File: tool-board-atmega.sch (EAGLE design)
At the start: 101 parts, among them IC3 ATMEGA2560-16AU, IC4 ATMEGA8U2-MU, Q1 16MHz, X1 22-23-2041, X2 MICROUSB_VERTICAL, X3 22-23-2041, X4 22-23-2041, Y2 16MHz

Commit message: board Rev01 done, needs review by Jaden and to clean up labels
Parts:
- removed U$2, U$3, U$4, U$5: FIDUCIALMOUNT, SmartPrj:FIDUCIALMOUNT
- added A: 22-23-2081, con-molex:22-23-2081
- added SV1, SV2, SV3: (no value), con-lstb:MA03-1
- added X5, X6: (no value), con-phoenix-254:MPT12
- added X7: (no value), con-phoenix-254:MPT4
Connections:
- new net N$50: A-1.S, IC3.(ADC7/TDI)PF7
- new net N$51: A-2.S, IC3.(ADC6/TDO)PF6
- new net N$52: A-3.S, IC3.(ADC5/TMS)PF5
- new net N$53: A-4.S, IC3.(ADC4/TCK)PF4
- new net N$56: A-5.S, IC3.(ADC3)PF3
- new net N$57: A-6.S, IC3.(ADC2)PF2
- new net N$58: A-7.S, IC3.(ADC1)PF1
- new net N$59: A-8.S, IC3.(ADC0)PF0
- new net N$60: SV1.2, X4-2.S
- new net N$61: SV2.2, X3-2.S
- new net N$62: SV3.2, X1-2.S
- net +12V: now also SV1.1, SV2.1, SV3.1, X6-10.1, X6-11.1, X6-12.1, X6-7.1, X6-8.1, X6-9.1
- net +24V: now also X7-1.1, X7-2.1, X7-3.1, X7-4.1
- net +5V: now also SV1.3, SV2.3, SV3.3, X6-1.1, X6-2.1, X6-3.1, X6-4.1, X6-5.1, X6-6.1; no longer X1-2.S, X3-2.S, X4-2.S
- net GND: now also X5-1.1, X5-10.1, X5-11.1, X5-12.1, X5-2.1, X5-3.1, X5-4.1, X5-5.1, X5-6.1, X5-7.1, X5-8.1, X5-9.1

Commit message: Made revisions of Jaden's review
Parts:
- removed RESET-EN: (no value), jumper:SJ
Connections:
- net RESET: no longer RESET-EN.1, RESET-EN.2
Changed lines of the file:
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@@
 <part name="GND28" library="supply1" deviceset="GND" device=""/>
 <part name="C7" library="SmartPrj" deviceset="C-EU" device="0603-RND" value="100n"/>
-<part name="RESET-EN" library="jumper" deviceset="SJ" device=""/>
 <part name="GND18" library="supply1" deviceset="GND" device=""/>
 <part name="C10" library="SmartPrj" deviceset="C-EU" device="0603-RND" value="1u"/>
@@
 <attribute name="VALUE" x="530.479" y="79.756" size="1.778" layer="96" rot="MR270"/>
 </instance>
-<instance part="RESET-EN" gate="1" x="538.48" y="96.52" smashed="yes">
-<attribute name="NAME" x="533.4" y="92.71" size="1.778" layer="95"/>
-<attribute name="VALUE" x="535.94" y="92.71" size="1.778" layer="96"/>
-</instance>
 <instance part="GND18" gate="1" x="510.54" y="58.42" smashed="yes">
 <attribute name="VALUE" x="508" y="55.88" size="1.778" layer="96"/>
@@
 </segment>
 <segment>
-<wire x1="530.86" y1="81.28" x2="533.4" y2="81.28" width="0.1524" layer="91"/>
-<wire x1="533.4" y1="81.28" x2="546.1" y2="81.28" width="0.1524" layer="91"/>
-<wire x1="546.1" y1="81.28" x2="548.64" y2="81.28" width="0.1524" layer="91"/>
-<wire x1="533.4" y1="96.52" x2="533.4" y2="81.28" width="0.1524" layer="91"/>
-<wire x1="543.56" y1="96.52" x2="546.1" y2="96.52" width="0.1524" layer="91"/>
-<wire x1="546.1" y1="96.52" x2="546.1" y2="81.28" width="0.1524" layer="91"/>
-<junction x="533.4" y="81.28"/>
-<junction x="546.1" y="81.28"/>
+<wire x1="530.86" y1="81.28" x2="548.64" y2="81.28" width="0.1524" layer="91"/>
 <label x="535.94" y="81.28" size="1.778" layer="95"/>
 <pinref part="C7" gate="G$1" pin="2"/>
-<pinref part="RESET-EN" gate="1" pin="1"/>
-<pinref part="RESET-EN" gate="1" pin="2"/>
 </segment>
 </net>

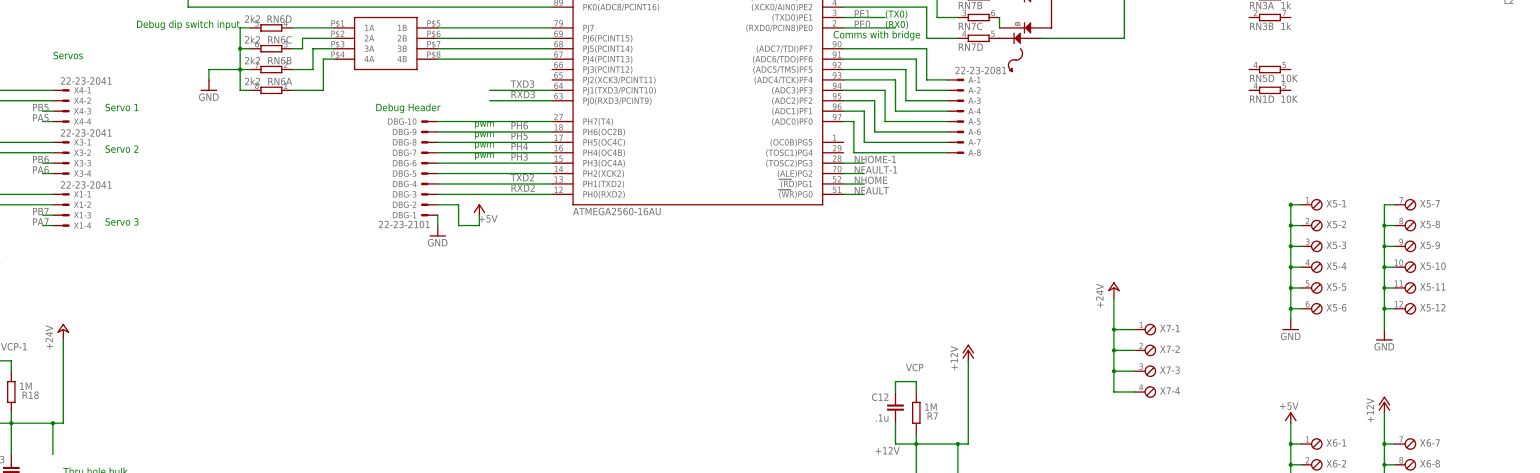
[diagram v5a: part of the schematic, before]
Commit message: working on labeling fixes
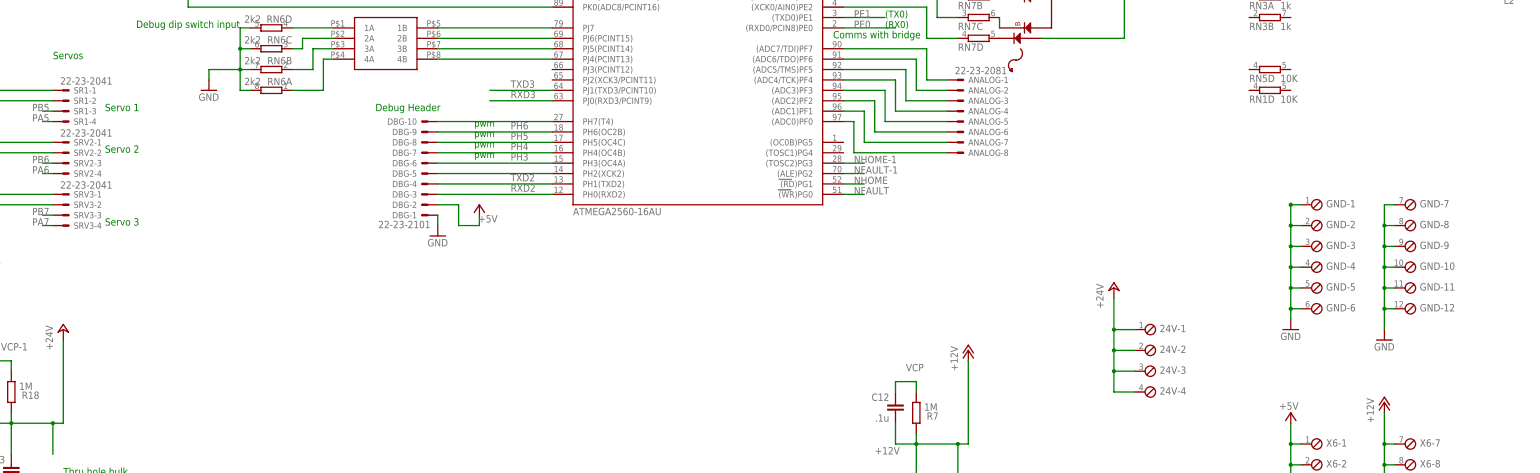
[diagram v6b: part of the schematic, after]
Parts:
- renumbered A to ANALOG, U$1 to STP1, X1 to SRV3, X3 to SRV2, X4 to SR1, X5 to GND, X7 to 24V

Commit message: REV 1.0
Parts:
- removed ON: GREEN, led:LEDCHIP-LED0805
- removed RN3: 1k, resistor-dil:4R-NCAY16
- removed U$7: DRV8825, ClinicalRobotics:DRV8825
- added 12, 24, 5: GREEN, led:LEDCHIP-LED0805
- added R23: 1k, SmartPrj:R-EU_R0603
- added R24: 5k1, SmartPrj:R-EU_R0603
- added R25: 2k2, SmartPrj:R-EU_R0603
- added STP2: DRV8825, ClinicalRobotics:DRV8825
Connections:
- removed net PA0: IC3.(AD0)PA0
- removed net PA1: IC3.(AD1)PA1
- removed net PA2: IC3.(AD2)PA2
- removed net PA3: IC3.(AD3)PA3
- removed net PA4: IC3.(AD4)PA4
- removed net PB0: IC3.(SS/PCINT0)PB0
- removed net PB4: IC3.(OC2A/PCINT4)PB4
- removed net PD7: IC3.(T0)PD7
- removed net RXD3: IC3.PJ0(RXD3/PCINT9)
- removed net TXD3: IC3.PJ1(TXD3/PCINT10)
- removed net USBVCC: IC4.UVCC
- new net N$64: 24.A, R24.2
- new net N$66: 12.A, R25.2
- net +12V: now also R25.1, STP2.VMA, STP2.VMB; no longer STP1.VMA, STP1.VMB
- net +24V: now also R24.1, STP1.VMA, STP1.VMB; no longer U$7.VMA, U$7.VMB
- net +5V: now also IC4.UVCC, R23.1; no longer RN3C.1
- net DECAY: now also STP2.DECAY; no longer STP1.DECAY
- net DECAY-1: now also STP1.DECAY; no longer U$7.DECAY
- net DIR: now also STP2.DIR; no longer STP1.DIR
- net DIR-1: now also STP1.DIR; no longer U$7.DIR
- net GND: now also 12.C, 24.C, 5.C, STP2.GND0, STP2.GND1, STP2.HEAT; no longer ON.C, U$7.GND0, U$7.GND1, U$7.HEAT
- net MODE0: now also STP2.MODE0; no longer STP1.MODE0
- net MODE0-1: now also STP1.MODE0; no longer U$7.MODE0
- net MODE1: now also STP2.MODE1; no longer STP1.MODE1
- net MODE1-1: now also STP1.MODE1; no longer U$7.MODE1
- net MODE2: now also STP2.MODE2; no longer STP1.MODE2
- net MODE2-1: now also STP1.MODE2; no longer U$7.MODE2
- net N$1: now also STP2.CP1; no longer STP1.CP1
- net N$12: now also STP2.BOUT2; no longer STP1.BOUT2
- net N$13: now also STP2.BOUT1; no longer STP1.BOUT1
- net N$14: now also STP2.V3P3OUT; no longer STP1.V3P3OUT
- net N$3: now also 5.A, R23.2; no longer ON.A, RN3C.2
- net N$37: now also STP1.ISENB; no longer U$7.ISENB
- net N$39: now also STP1.CP1; no longer U$7.CP1
- net N$4: now also STP2.CP2; no longer STP1.CP2
- net N$40: now also STP1.CP2; no longer U$7.CP2
- net N$41: now also STP1.V3P3OUT; no longer U$7.V3P3OUT
- net N$42: now also STP1.AVREF, STP1.BVREF; no longer U$7.AVREF, U$7.BVREF
- net N$43: now also STP1.AOUT1; no longer U$7.AOUT1
- net N$44: now also STP1.AOUT2; no longer U$7.AOUT2
- net N$45: now also STP1.BOUT2; no longer U$7.BOUT2
- net N$46: now also STP1.BOUT1; no longer U$7.BOUT1
- net N$47: now also STP1.ISENA; no longer U$7.ISENA
- net N$48: now also STP2.ISENA; no longer STP1.ISENA
- net N$49: now also STP2.ISENB; no longer STP1.ISENB
- net N$6: now also STP2.AVREF, STP2.BVREF; no longer STP1.AVREF, STP1.BVREF
- net N$7: now also STP2.AOUT1; no longer STP1.AOUT1
- net N$8: now also STP2.AOUT2; no longer STP1.AOUT2
- net NENBL: now also STP2.NENBL; no longer STP1.NENBL
- net NENBL-1: now also STP1.NENBL; no longer U$7.NENBL
- net NFAULT: now also STP2.NFAULT; no longer STP1.NFAULT
- net NFAULT-1: now also STP1.NFAULT; no longer U$7.NFAULT
- net NHOME: now also STP2.NHOME; no longer STP1.NHOME
- net NHOME-1: now also STP1.NHOME; no longer U$7.NHOME
- net NRESET: now also STP2.NRESET; no longer STP1.NRESET
- net NRESET-1: now also STP1.NRESET; no longer U$7.NRESET
- net NSLEEP: now also STP2.NSLEEP; no longer STP1.NSLEEP
- net NSLEEP-1: now also STP1.NSLEEP; no longer U$7.NSLEEP
- net NSTEP: now also STP2.STEP; no longer STP1.STEP
- net NSTEP-1: now also STP1.STEP; no longer U$7.STEP
- net VCP: now also STP2.VCP; no longer STP1.VCP
- net VCP-1: now also STP1.VCP; no longer U$7.VCP
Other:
- note removed: "Need to calc resistor values"
- moved on the sheet: RESET
